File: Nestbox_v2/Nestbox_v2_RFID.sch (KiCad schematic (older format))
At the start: 8 parts, among them J701 CONN_01X05, Q701 Q_NMOS_DGS

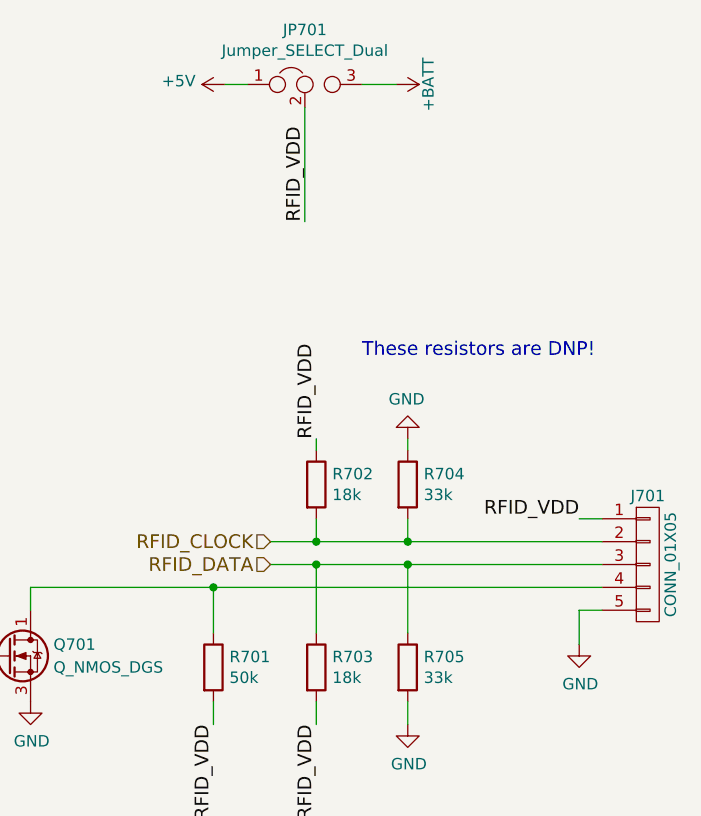
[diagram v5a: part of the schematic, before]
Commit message: correct size of the PCB drawn with connector arrangement done as well
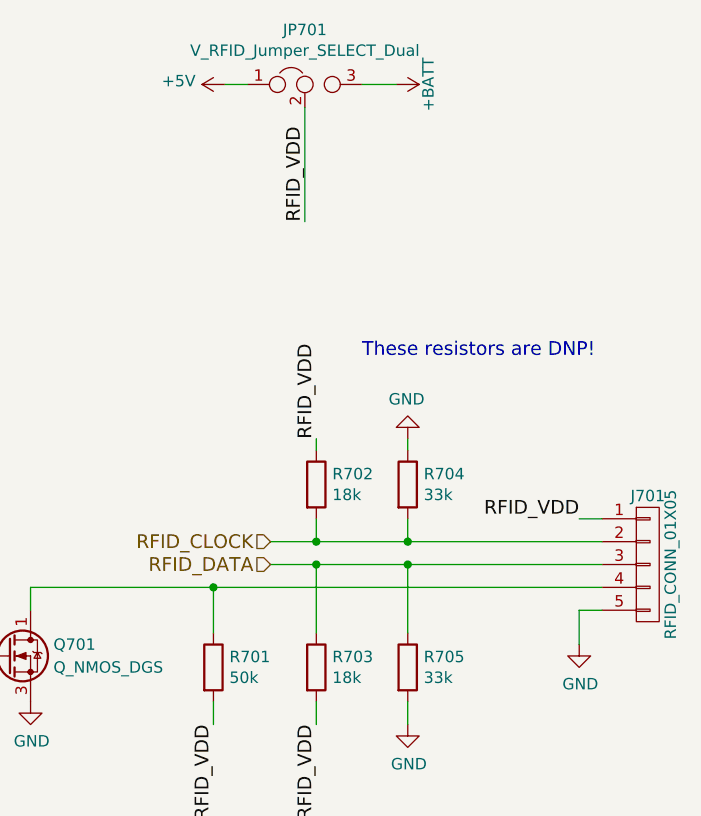
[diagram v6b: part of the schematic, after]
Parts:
- J701: value CONN_01X05 -> RFID_CONN_01X05
- JP701: value Jumper_SELECT_Dual -> V_RFID_Jumper_SELECT_Dual
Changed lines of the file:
@@
 P 5550 2300
 F 0 "JP701" H 5550 2539 50  0000 C CNN
-F 1 "Jumper_SELECT_Dual" H 5550 2448 50  0000 C CNN
+F 1 "V_RFID_Jumper_SELECT_Dual" H 5550 2448 50  0000 C CNN
 F 2 "Pin_Headers:Pin_Header_Straight_1x03_Pitch2.54mm" H 5550 2300 50  0001 C CNN
 F 3 "" H 5550 2300 50  0001 C CNN
@@
 RFID_VDD
 $Comp
-L +5V #PWR085
+L +5V #PWR702
 U 1 1 5A0305A8
 P 5200 2300
-F 0 "#PWR085" H 5200 2150 50  0001 C CNN
+F 0 "#PWR702" H 5200 2150 50  0001 C CNN
 F 1 "+5V" V 5215 2428 50  0000 L CNN
 F 2 "" H 5200 2300 50  0001 C CNN
@@
 $EndComp
 $Comp
-L GND #PWR086
+L GND #PWR704
 U 1 1 5AF8ABAA
 P 6000 3850
-F 0 "#PWR086" H 6000 3600 50  0001 C CNN
+F 0 "#PWR704" H 6000 3600 50  0001 C CNN
 F 1 "GND" H 6005 3677 50  0000 C CNN
 F 2 "" H 6000 3850 50  0001 C CNN
@@
 $EndComp
 $Comp
-L GND #PWR087
+L GND #PWR705
 U 1 1 5AF8AC8E
 P 6000 5100
-F 0 "#PWR087" H 6000 4850 50  0001 C CNN
+F 0 "#PWR705" H 6000 4850 50  0001 C CNN
 F 1 "GND" H 6005 4927 50  0000 C CNN
 F 2 "" H 6000 5100 50  0001 C CNN
@@
 RFID_VDD
 $Comp
-L GND #PWR088
+L GND #PWR706
 U 1 1 5AF8B903
 P 6750 4750
-F 0 "#PWR088" H 6750 4500 50  0001 C CNN
+F 0 "#PWR706" H 6750 4500 50  0001 C CNN
 F 1 "GND" H 6755 4577 50  0000 C CNN
 F 2 "" H 6750 4750 50  0001 C CNN
@@
 	5150 5100 5150 5000
 $Comp
-L GND #PWR089
+L GND #PWR701
 U 1 1 5B088780
 P 4350 5000
-F 0 "#PWR089" H 4350 4750 50  0001 C CNN
+F 0 "#PWR701" H 4350 4750 50  0001 C CNN
 F 1 "GND" H 4355 4827 50  0000 C CNN
 F 2 "" H 4350 5000 50  0001 C CNN
@@
 P 7050 4400
 F 0 "J701" H 7050 4700 50  0000 C CNN
-F 1 "CONN_01X05" V 7150 4400 50  0000 C CNN
+F 1 "RFID_CONN_01X05" V 7150 4400 50  0000 C CNN
 F 2 "Terminal_Blocks:TerminalBlock_Pheonix_PT-3.5mm_5pol" H 7050 4400 50  0001 C CNN
 F 3 "" H 7050 4400 50  0001 C CNN
@@
 	5200 2300 5300 2300
 $Comp
-L +BATT #PWR090
+L +BATT #PWR703
 U 1 1 5B08AE2C
 P 5950 2300
-F 0 "#PWR090" H 5950 2150 50  0001 C CNN
+F 0 "#PWR703" H 5950 2150 50  0001 C CNN
 F 1 "+BATT" H 5950 2440 50  0000 C CNN
 F 2 "" H 5950 2300 50  0001 C CNN

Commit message: all footprints assigned except mosfets; final connectors and their locatino, started component placement
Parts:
- J701: footprint Terminal_Blocks:TerminalBlock_Pheonix_PT-3.5mm_5pol -> Terminal_Blocks:TerminalBlock_Pheonix_MPT-2.54mm_5pol
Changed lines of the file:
@@
 EESchema Schematic File Version 2
-LIBS:Nestbox_v2-rescue
-LIBS:Octanis3
 LIBS:power
 LIBS:device
-LIBS:switches
-LIBS:relays
-LIBS:motors
 LIBS:transistors
 LIBS:conn
@@
 LIBS:contrib
 LIBS:valves
-LIBS:SeeedOPL-Capacitor-2016
-LIBS:SeeedOPL-Connector-2016
-LIBS:SeeedOPL-Crystal Oscillator-2016
-LIBS:SeeedOPL-Diode-2016
-LIBS:SeeedOPL-Display-2016
-LIBS:SeeedOPL-Fuse-2016
-LIBS:SeeedOPL-IC-2016
-LIBS:SeeedOPL-Inductor-2016
-LIBS:SeeedOPL-LED-2016
-LIBS:SeeedOPL-Relay-2016
-LIBS:SeeedOPL-Resistor-2016
-LIBS:SeeedOPL-Sensor-2016
-LIBS:SeeedOPL-Switch-2016
-LIBS:SeeedOPL-Transistor-2016
+LIBS:Octanis3
 LIBS:Nestbox_v2-cache
 EELAYER 25 0
@@
 RFID_VDD
 $Comp
-L +5V #PWR702
+L +5V #PWR071
 U 1 1 5A0305A8
 P 5200 2300
-F 0 "#PWR702" H 5200 2150 50  0001 C CNN
+F 0 "#PWR071" H 5200 2150 50  0001 C CNN
 F 1 "+5V" V 5215 2428 50  0000 L CNN
 F 2 "" H 5200 2300 50  0001 C CNN
@@
 $EndComp
 $Comp
-L GND #PWR704
+L GND #PWR072
 U 1 1 5AF8ABAA
 P 6000 3850
-F 0 "#PWR704" H 6000 3600 50  0001 C CNN
+F 0 "#PWR072" H 6000 3600 50  0001 C CNN
 F 1 "GND" H 6005 3677 50  0000 C CNN
 F 2 "" H 6000 3850 50  0001 C CNN
@@
 $EndComp
 $Comp
-L GND #PWR705
+L GND #PWR073
 U 1 1 5AF8AC8E
 P 6000 5100
-F 0 "#PWR705" H 6000 4850 50  0001 C CNN
+F 0 "#PWR073" H 6000 4850 50  0001 C CNN
 F 1 "GND" H 6005 4927 50  0000 C CNN
 F 2 "" H 6000 5100 50  0001 C CNN
@@
 RFID_VDD
 $Comp
-L GND #PWR706
+L GND #PWR074
 U 1 1 5AF8B903
 P 6750 4750
-F 0 "#PWR706" H 6750 4500 50  0001 C CNN
+F 0 "#PWR074" H 6750 4500 50  0001 C CNN
 F 1 "GND" H 6755 4577 50  0000 C CNN
 F 2 "" H 6750 4750 50  0001 C CNN
@@
 	5150 5100 5150 5000
 $Comp
-L GND #PWR701
+L GND #PWR075
 U 1 1 5B088780
 P 4350 5000
-F 0 "#PWR701" H 4350 4750 50  0001 C CNN
+F 0 "#PWR075" H 4350 4750 50  0001 C CNN
 F 1 "GND" H 4355 4827 50  0000 C CNN
 F 2 "" H 4350 5000 50  0001 C CNN
@@
 F 0 "J701" H 7050 4700 50  0000 C CNN
 F 1 "RFID_CONN_01X05" V 7150 4400 50  0000 C CNN
-F 2 "Terminal_Blocks:TerminalBlock_Pheonix_PT-3.5mm_5pol" H 7050 4400 50  0001 C CNN
+F 2 "Terminal_Blocks:TerminalBlock_Pheonix_MPT-2.54mm_5pol" H 7050 4400 50  0001 C CNN
 F 3 "" H 7050 4400 50  0001 C CNN
 	1    7050 4400
@@
 	5200 2300 5300 2300
 $Comp
-L +BATT #PWR703
+L +BATT #PWR076
 U 1 1 5B08AE2C
 P 5950 2300
-F 0 "#PWR703" H 5950 2150 50  0001 C CNN
+F 0 "#PWR076" H 5950 2150 50  0001 C CNN
 F 1 "+BATT" H 5950 2440 50  0000 C CNN
 F 2 "" H 5950 2300 50  0001 C CNN

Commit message: finished component placement
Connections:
- net RFID_CLOCK: now also R702.1; no longer J701.2 (P2), R702.2
- net RFID_DATA: now also R703.2; no longer J701.3 (P3), R703.1
- net RFID_VDD: no longer R702.1, R703.2
- new net: J701.2 (P2), R702.2
- new net: J701.3 (P3), R703.1
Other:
- moved on the sheet: R704, R705
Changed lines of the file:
@@
 RFID_VDD
 $Comp
-L +5V #PWR071
+L +5V #PWR070
 U 1 1 5A0305A8
 P 5200 2300
-F 0 "#PWR071" H 5200 2150 50  0001 C CNN
+F 0 "#PWR070" H 5200 2150 50  0001 C CNN
 F 1 "+5V" V 5215 2428 50  0000 L CNN
 F 2 "" H 5200 2300 50  0001 C CNN
@@
 L R R704
 U 1 1 5AF8AAF5
-P 6000 4050
-F 0 "R704" H 6070 4096 50  0000 L CNN
-F 1 "33k" H 6070 4005 50  0000 L CNN
-F 2 "Resistors_SMD:R_0603" V 5930 4050 50  0001 C CNN
-F 3 "" H 6000 4050 50  0001 C CNN
-	1    6000 4050
+P 5600 3650
+F 0 "R704" H 5670 3696 50  0000 L CNN
+F 1 "33k" H 5670 3605 50  0000 L CNN
+F 2 "Resistors_SMD:R_0603" V 5530 3650 50  0001 C CNN
+F 3 "" H 5600 3650 50  0001 C CNN
+	1    5600 3650
 	1    0    0    -1
 $EndComp
@@
 L R R705
 U 1 1 5AF8AB4E
-P 6000 4850
-F 0 "R705" H 6070 4896 50  0000 L CNN
-F 1 "33k" H 6070 4805 50  0000 L CNN
-F 2 "Resistors_SMD:R_0603" V 5930 4850 50  0001 C CNN
-F 3 "" H 6000 4850 50  0001 C CNN
-	1    6000 4850
-	1    0    0    -1
+P 5600 5550
+F 0 "R705" H 5670 5596 50  0000 L CNN
+F 1 "33k" H 5670 5505 50  0000 L CNN
+F 2 "Resistors_SMD:R_0603" V 5530 5550 50  0001 C CNN
+F 3 "" H 5600 5550 50  0001 C CNN
+	1    5600 5550
+	1    0    0    -1
+$EndComp
+$Comp
+L GND #PWR071
+U 1 1 5AF8ABAA
+P 5600 3450
+F 0 "#PWR071" H 5600 3200 50  0001 C CNN
+F 1 "GND" H 5605 3277 50  0000 C CNN
+F 2 "" H 5600 3450 50  0001 C CNN
+F 3 "" H 5600 3450 50  0001 C CNN
+	1    5600 3450
+	-1   0    0    1
 $EndComp
 $Comp
 L GND #PWR072
-U 1 1 5AF8ABAA
-P 6000 3850
-F 0 "#PWR072" H 6000 3600 50  0001 C CNN
-F 1 "GND" H 6005 3677 50  0000 C CNN
-F 2 "" H 6000 3850 50  0001 C CNN
-F 3 "" H 6000 3850 50  0001 C CNN
-	1    6000 3850
-	-1   0    0    1
+U 1 1 5AF8AC8E
+P 5600 5800
+F 0 "#PWR072" H 5600 5550 50  0001 C CNN
+F 1 "GND" H 5605 5627 50  0000 C CNN
+F 2 "" H 5600 5800 50  0001 C CNN
+F 3 "" H 5600 5800 50  0001 C CNN
+	1    5600 5800
+	1    0    0    -1
 $EndComp
 $Comp
 L GND #PWR073
-U 1 1 5AF8AC8E
-P 6000 5100
-F 0 "#PWR073" H 6000 4850 50  0001 C CNN
-F 1 "GND" H 6005 4927 50  0000 C CNN
-F 2 "" H 6000 5100 50  0001 C CNN
-F 3 "" H 6000 5100 50  0001 C CNN
-	1    6000 5100
-	1    0    0    -1
-$EndComp
-Wire Wire Line
-	6000 5000 6000 5100
-Wire Wire Line
-	6000 3900 6000 3850
-Connection ~ 6000 4400
-Wire Wire Line
-	6000 4400 6000 4700
-Connection ~ 6000 4300
-Wire Wire Line
-	6000 4300 6000 4200
-Wire Wire Line
-	5600 5000 5600 5100
-Wire Wire Line
-	5600 3850 5600 3900
-Connection ~ 5600 4300
-Wire Wire Line
-	5600 4300 5600 4200
-Connection ~ 5600 4400
-Wire Wire Line
-	5600 4400 5600 4700
-Wire Wire Line
-	5400 4400 6850 4400
-Wire Wire Line
-	5400 4300 6850 4300
-Wire Wire Line
-	6750 4200 6850 4200
-Wire Wire Line
-	5550 2400 5550 2900
-Text Label 5600 3850 1    60   ~ 0
-RFID_VDD
-Text Label 5600 5100 3    60   ~ 0
-RFID_VDD
-$Comp
-L GND #PWR074
 U 1 1 5AF8B903
 P 6750 4750
-F 0 "#PWR074" H 6750 4500 50  0001 C CNN
+F 0 "#PWR073" H 6750 4500 50  0001 C CNN
 F 1 "GND" H 6755 4577 50  0000 C CNN
 F 2 "" H 6750 4750 50  0001 C CNN
@@
 	1    0    0    -1
 $EndComp
-Text HLabel 5400 4400 0    60   Input ~ 0
+Text HLabel 5700 5200 2    60   Input ~ 0
 RFID_DATA
-Text HLabel 5400 4300 0    60   Input ~ 0
+Text HLabel 5450 3850 0    60   Input ~ 0
 RFID_CLOCK
-Text Notes 5800 3500 0    60   ~ 0
+Text Notes 7150 3550 0    60   ~ 0
 These resistors are DNP!\n
 $Comp
@@
 Text Label 5150 5100 3    60   ~ 0
 RFID_VDD
-Wire Wire Line
-	5150 5100 5150 5000
-$Comp
-L GND #PWR075
+$Comp
+L GND #PWR074
 U 1 1 5B088780
 P 4350 5000
-F 0 "#PWR075" H 4350 4750 50  0001 C CNN
+F 0 "#PWR074" H 4350 4750 50  0001 C CNN
 F 1 "GND" H 4355 4827 50  0000 C CNN
 F 2 "" H 4350 5000 50  0001 C CNN
@@
 Text HLabel 4000 4800 0    60   Input ~ 0
 RFID_SLEEP_N
-Wire Wire Line
-	4000 4800 4050 4800
-Wire Wire Line
-	4350 4600 4350 4500
-Wire Wire Line
-	4350 4500 6850 4500
 $Comp
 L R R701
@@
 	1    0    0    -1
 $EndComp
-Wire Wire Line
-	5150 4700 5150 4500
-Connection ~ 5150 4500
-Wire Wire Line
-	6750 4600 6850 4600
 $Comp
 L CONN_01X05 J701
@@
 	1    0    0    -1
 $EndComp
-Wire Wire Line
-	6750 4750 6750 4600
-Wire Wire Line
-	5800 2300 5950 2300
-Wire Wire Line
-	5200 2300 5300 2300
-$Comp
-L +BATT #PWR076
+$Comp
+L +BATT #PWR075
 U 1 1 5B08AE2C
 P 5950 2300
-F 0 "#PWR076" H 5950 2150 50  0001 C CNN
+F 0 "#PWR075" H 5950 2150 50  0001 C CNN
 F 1 "+BATT" H 5950 2440 50  0000 C CNN
 F 2 "" H 5950 2300 50  0001 C CNN
@@
 	0    1    1    0
 $EndComp
+Wire Wire Line
+	5600 5700 5600 5800
+Wire Wire Line
+	5600 3500 5600 3450
+Wire Wire Line
+	5600 5000 5600 5400
+Wire Wire Line
+	5600 3800 5600 3900
+Wire Wire Line
+	6750 4200 6850 4200
+Wire Wire Line
+	5550 2400 5550 2900
+Wire Wire Line
+	5150 5100 5150 5000
+Wire Wire Line
+	4000 4800 4050 4800
+Wire Wire Line
+	4350 4600 4350 4500
+Wire Wire Line
+	4350 4500 6850 4500
+Wire Wire Line
+	5150 4700 5150 4500
+Connection ~ 5150 4500
+Wire Wire Line
+	6750 4600 6850 4600
+Wire Wire Line
+	6750 4750 6750 4600
+Wire Wire Line
+	5800 2300 5950 2300
+Wire Wire Line
+	5200 2300 5300 2300
+Wire Wire Line
+	5450 3850 5600 3850
+Connection ~ 5600 3850
+Wire Wire Line
+	5700 5200 5600 5200
+Connection ~ 5600 5200
+Wire Wire Line
+	6850 4300 5600 4300
+Wire Wire Line
+	5600 4300 5600 4200
+Wire Wire Line
+	6850 4400 5600 4400
+Wire Wire Line
+	5600 4400 5600 4700
 $EndSCHEMATC
